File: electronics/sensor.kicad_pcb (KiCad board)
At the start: 2 copper layers, 98 x 52.8 mm, 3 parts, among them P1 SENSOR, U1 AH1815

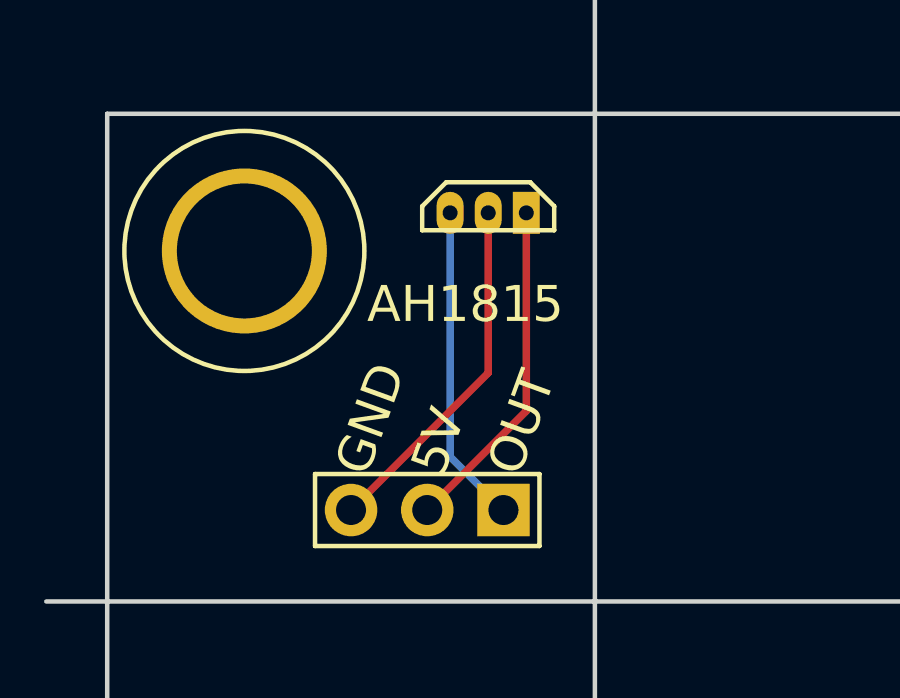
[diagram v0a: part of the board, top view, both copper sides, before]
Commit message: Sensor PCB panelization tweaks; update README and travis config
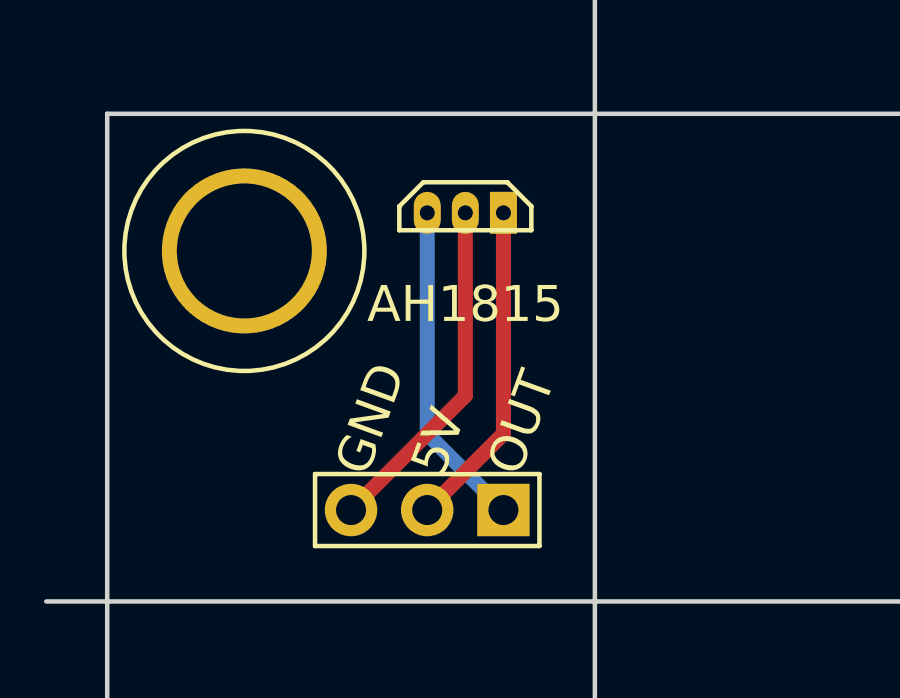
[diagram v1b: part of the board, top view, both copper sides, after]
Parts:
- moved U1 0.76 mm to (31.9, 23.3)
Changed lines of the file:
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@@
     (links 3)
     (no_connects 0)
-    (area 17.892999 15.098999 116.075001 68.075001)
+    (area 10.070287 15.098999 116.075001 68.075001)
     (thickness 1.6)
-    (drawings 8)
+    (drawings 10)
     (tracks 6)
     (zones 0)
@@
     (nets 4)
   )
-  (page User 150.012 119.99)
+  (page User 150.012 140.005)
   (title_block
     (title "Splitflap sensor board")
@@
   )
   (module ah1815:AH1815 (layer B.Cu)
-    (at 32.7 23.302 180)
+    (at 31.938 23.302 180)
     (fp_text reference U1 (at 5.08 1.27 180) (layer B.SilkS) hide
       (effects (font (size 1 1) (thickness 0.15)) (justify mirror))
@@
       (net 3 "Net-(P1-Pad1)"))
   )
+  (dimension 8.636 (width 0.3) (layer Cmts.User)
+    (gr_text "8.636 mm" (at 28.89 41.844) (layer Cmts.User)
+      (effects (font (size 1.5 1.5) (thickness 0.3)))
+    )
+    (feature1 (pts (xy 33.208 33.208) (xy 33.208 40.734)))
+    (feature2 (pts (xy 24.572 33.208) (xy 24.572 40.734)))
+    (crossbar (pts (xy 24.572 38.034) (xy 33.208 38.034)))
+    (arrow1a (pts (xy 33.208 38.034) (xy 32.081496 38.620421)))
+    (arrow1b (pts (xy 33.208 38.034) (xy 32.081496 37.447579)))
+    (arrow2a (pts (xy 24.572 38.034) (xy 25.698504 38.620421)))
+    (arrow2b (pts (xy 24.572 38.034) (xy 25.698504 37.447579)))
+  )
+  (dimension 8.636 (width 0.3) (layer Cmts.User)
+    (gr_text "8.636 mm" (at 13.396 28.89 270) (layer Cmts.User)
+      (effects (font (size 1.5 1.5) (thickness 0.3)))
+    )
+    (feature1 (pts (xy 24.572 33.208) (xy 14.506 33.208)))
+    (feature2 (pts (xy 24.572 24.572) (xy 14.506 24.572)))
+    (crossbar (pts (xy 17.206 24.572) (xy 17.206 33.208)))
+    (arrow1a (pts (xy 17.206 33.208) (xy 16.619579 32.081496)))
+    (arrow1b (pts (xy 17.206 33.208) (xy 17.792421 32.081496)))
+    (arrow2a (pts (xy 17.206 24.572) (xy 16.619579 25.698504)))
+    (arrow2b (pts (xy 17.206 24.572) (xy 17.792421 25.698504)))
+  )
   (gr_line (start 20 20) (end 116 20) (angle 90) (layer Edge.Cuts) (width 0.15))
   (gr_text AH1815 (at 31.938 26.35) (layer F.SilkS)
@@
   (gr_line (start 17.968 36.256) (end 73.848 36.256) (angle 90) (layer Edge.Cuts) (width 0.15))
   (gr_line (start 20 68) (end 20 20) (angle 90) (layer Edge.Cuts) (width 0.15))
-  (segment (start 32.7 23.302) (end 32.7 28.636) (width 0.25) (layer F.Cu) (net 1))
-  (segment (start 32.7 28.636) (end 28.128 33.208) (width 0.25) (layer F.Cu) (net 1))
-  (segment (start 33.97 23.302) (end 33.97 29.906) (width 0.25) (layer F.Cu) (net 2))
-  (segment (start 33.97 29.906) (end 30.668 33.208) (width 0.25) (layer F.Cu) (net 2))
-  (segment (start 31.43 23.302) (end 31.43 31.43) (width 0.25) (layer B.Cu) (net 3))
-  (segment (start 31.43 31.43) (end 33.208 33.208) (width 0.25) (layer B.Cu) (net 3))
+  (segment (start 31.938 23.302) (end 31.938 29.398) (width 0.5) (layer F.Cu) (net 1) (status 10))
+  (segment (start 31.938 29.398) (end 28.128 33.208) (width 0.5) (layer F.Cu) (net 1) (status 20))
+  (segment (start 33.208 23.302) (end 33.208 30.668) (width 0.5) (layer F.Cu) (net 2) (status 10))
+  (segment (start 33.208 30.668) (end 30.668 33.208) (width 0.5) (layer F.Cu) (net 2) (status 20))
+  (segment (start 33.208 33.208) (end 30.668 30.668) (width 0.5) (layer B.Cu) (net 3) (status 10))
+  (segment (start 30.668 30.668) (end 30.668 23.302) (width 0.5) (layer B.Cu) (net 3) (status 20))
 )

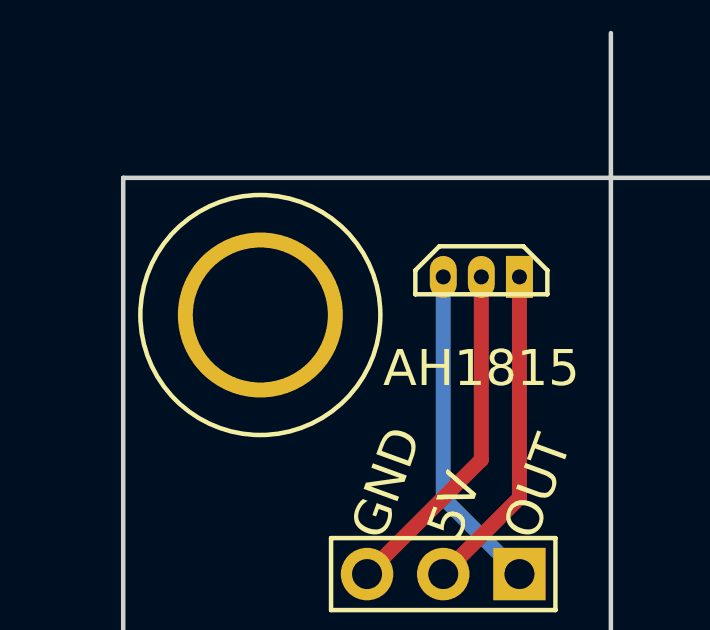
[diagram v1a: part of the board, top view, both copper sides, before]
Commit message: Sensor PCB: more dimension labels, commit/date text
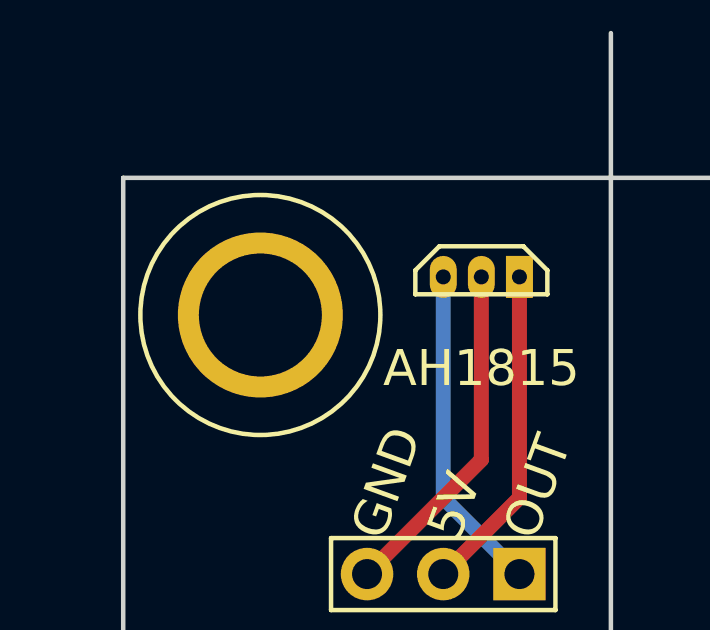
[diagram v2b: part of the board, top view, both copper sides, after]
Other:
- board text added: "COMMIT: deadbeef DATE: YYYY-MM-DD"
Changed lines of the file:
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@@
     (links 3)
     (no_connects 0)
-    (area 10.070287 15.098999 116.075001 68.075001)
+    (area 7.610287 15.098999 116.075001 68.075001)
     (thickness 1.6)
-    (drawings 10)
+    (drawings 15)
     (tracks 6)
     (zones 0)
@@
     (mod_text_size 1 1)
     (mod_text_width 0.15)
-    (pad_size 9 5.5)
-    (pad_drill 8)
+    (pad_size 5.5 5.5)
+    (pad_drill 4.1)
     (pad_to_mask_clearance 0.2)
     (aux_axis_origin 0 0)
@@
     )
     (fp_circle (center 0 0) (end 4 0) (layer F.SilkS) (width 0.15))
-    (pad 1 thru_hole circle (at 0 0) (size 5.5 5.5) (drill 4.5) (layers *.Cu *.Mask F.SilkS)
+    (pad 1 thru_hole circle (at 0 0) (size 5.5 5.5) (drill 4.1) (layers *.Cu *.Mask F.SilkS)
       (clearance 1.5))
   )
@@
       (net 3 "Net-(P1-Pad1)"))
   )
+  (gr_text "COMMIT: deadbeef\nDATE: YYYY-MM-DD" (at 35.494 31.684) (layer B.SilkS)
+    (effects (font (size 1 0.9) (thickness 0.2)) (justify left mirror))
+  )
+  (dimension 8.636 (width 0.3) (layer Cmts.User)
+    (gr_text "8.636 mm" (at 16.364 28.89 90) (layer Cmts.User)
+      (effects (font (size 1.5 1.5) (thickness 0.3)))
+    )
+    (feature1 (pts (xy 24.572 24.572) (xy 15.014 24.572)))
+    (feature2 (pts (xy 24.572 33.208) (xy 15.014 33.208)))
+    (crossbar (pts (xy 17.714 33.208) (xy 17.714 24.572)))
+    (arrow1a (pts (xy 17.714 24.572) (xy 18.300421 25.698504)))
+    (arrow1b (pts (xy 17.714 24.572) (xy 17.127579 25.698504)))
+    (arrow2a (pts (xy 17.714 33.208) (xy 18.300421 32.081496)))
+    (arrow2b (pts (xy 17.714 33.208) (xy 17.127579 32.081496)))
+  )
+  (dimension 4.572 (width 0.3) (layer Cmts.User)
+    (gr_text "4.572 mm" (at 7.3 22.286 90) (layer Cmts.User)
+      (effects (font (size 1.5 1.5) (thickness 0.3)))
+    )
+    (feature1 (pts (xy 24.572 20) (xy 8.156 20)))
+    (feature2 (pts (xy 24.572 24.572) (xy 8.156 24.572)))
+    (crossbar (pts (xy 10.856 24.572) (xy 10.856 20)))
+    (arrow1a (pts (xy 10.856 20) (xy 11.442421 21.126504)))
+    (arrow1b (pts (xy 10.856 20) (xy 10.269579 21.126504)))
+    (arrow2a (pts (xy 10.856 24.572) (xy 11.442421 23.445496)))
+    (arrow2b (pts (xy 10.856 24.572) (xy 10.269579 23.445496)))
+  )
+  (dimension 4.572 (width 0.3) (layer Cmts.User)
+    (gr_text "4.572 mm" (at 22.286 8.57) (layer Cmts.User)
+      (effects (font (size 1.5 1.5) (thickness 0.3)))
+    )
+    (feature1 (pts (xy 20 24.572) (xy 20 9.68)))
+    (feature2 (pts (xy 24.572 24.572) (xy 24.572 9.68)))
+    (crossbar (pts (xy 24.572 12.38) (xy 20 12.38)))
+    (arrow1a (pts (xy 20 12.38) (xy 21.126504 11.793579)))
+    (arrow1b (pts (xy 20 12.38) (xy 21.126504 12.966421)))
+    (arrow2a (pts (xy 24.572 12.38) (xy 23.445496 11.793579)))
+    (arrow2b (pts (xy 24.572 12.38) (xy 23.445496 12.966421)))
+  )
+  (dimension 7.366 (width 0.3) (layer Cmts.User)
+    (gr_text "7.366 mm" (at 28.382 14.412) (layer Cmts.User)
+      (effects (font (size 1.5 1.5) (thickness 0.3)))
+    )
+    (feature1 (pts (xy 31.938 24.572) (xy 31.938 15.522)))
+    (feature2 (pts (xy 24.572 24.572) (xy 24.572 15.522)))
+    (crossbar (pts (xy 24.572 18.222) (xy 31.938 18.222)))
+    (arrow1a (pts (xy 31.938 18.222) (xy 30.811496 18.808421)))
+    (arrow1b (pts (xy 31.938 18.222) (xy 30.811496 17.635579)))
+    (arrow2a (pts (xy 24.572 18.222) (xy 25.698504 18.808421)))
+    (arrow2b (pts (xy 24.572 18.222) (xy 25.698504 17.635579)))
+  )
+  (dimension 1.27 (width 0.3) (layer Cmts.User)
+    (gr_text "1.270 mm" (at 40.828 24.064 90) (layer Cmts.User)
+      (effects (font (size 1.5 1.5) (thickness 0.3)))
+    )
+    (feature1 (pts (xy 24.572 23.302) (xy 39.718 23.302)))
+    (feature2 (pts (xy 24.572 24.572) (xy 39.718 24.572)))
+    (crossbar (pts (xy 37.018 24.572) (xy 37.018 23.302)))
+    (arrow1a (pts (xy 37.018 23.302) (xy 37.604421 24.428504)))
+    (arrow1b (pts (xy 37.018 23.302) (xy 36.431579 24.428504)))
+    (arrow2a (pts (xy 37.018 24.572) (xy 37.604421 23.445496)))
+    (arrow2b (pts (xy 37.018 24.572) (xy 36.431579 23.445496)))
+  )
   (dimension 8.636 (width 0.3) (layer Cmts.User)
     (gr_text "8.636 mm" (at 28.89 41.844) (layer Cmts.User)
@@
     (arrow2b (pts (xy 24.572 38.034) (xy 25.698504 37.447579)))
   )
-  (dimension 8.636 (width 0.3) (layer Cmts.User)
-    (gr_text "8.636 mm" (at 13.396 28.89 270) (layer Cmts.User)
-      (effects (font (size 1.5 1.5) (thickness 0.3)))
-    )
-    (feature1 (pts (xy 24.572 33.208) (xy 14.506 33.208)))
-    (feature2 (pts (xy 24.572 24.572) (xy 14.506 24.572)))
-    (crossbar (pts (xy 17.206 24.572) (xy 17.206 33.208)))
-    (arrow1a (pts (xy 17.206 33.208) (xy 16.619579 32.081496)))
-    (arrow1b (pts (xy 17.206 33.208) (xy 17.792421 32.081496)))
-    (arrow2a (pts (xy 17.206 24.572) (xy 16.619579 25.698504)))
-    (arrow2b (pts (xy 17.206 24.572) (xy 17.792421 25.698504)))
-  )
   (gr_line (start 20 20) (end 116 20) (angle 90) (layer Edge.Cuts) (width 0.15))
